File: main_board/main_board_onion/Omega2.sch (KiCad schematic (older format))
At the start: 25 parts, among them J16 RJ45, J17 USB_B_Micro_Omega, U4 H1102, U5 CP2102N-A01-GQFN24

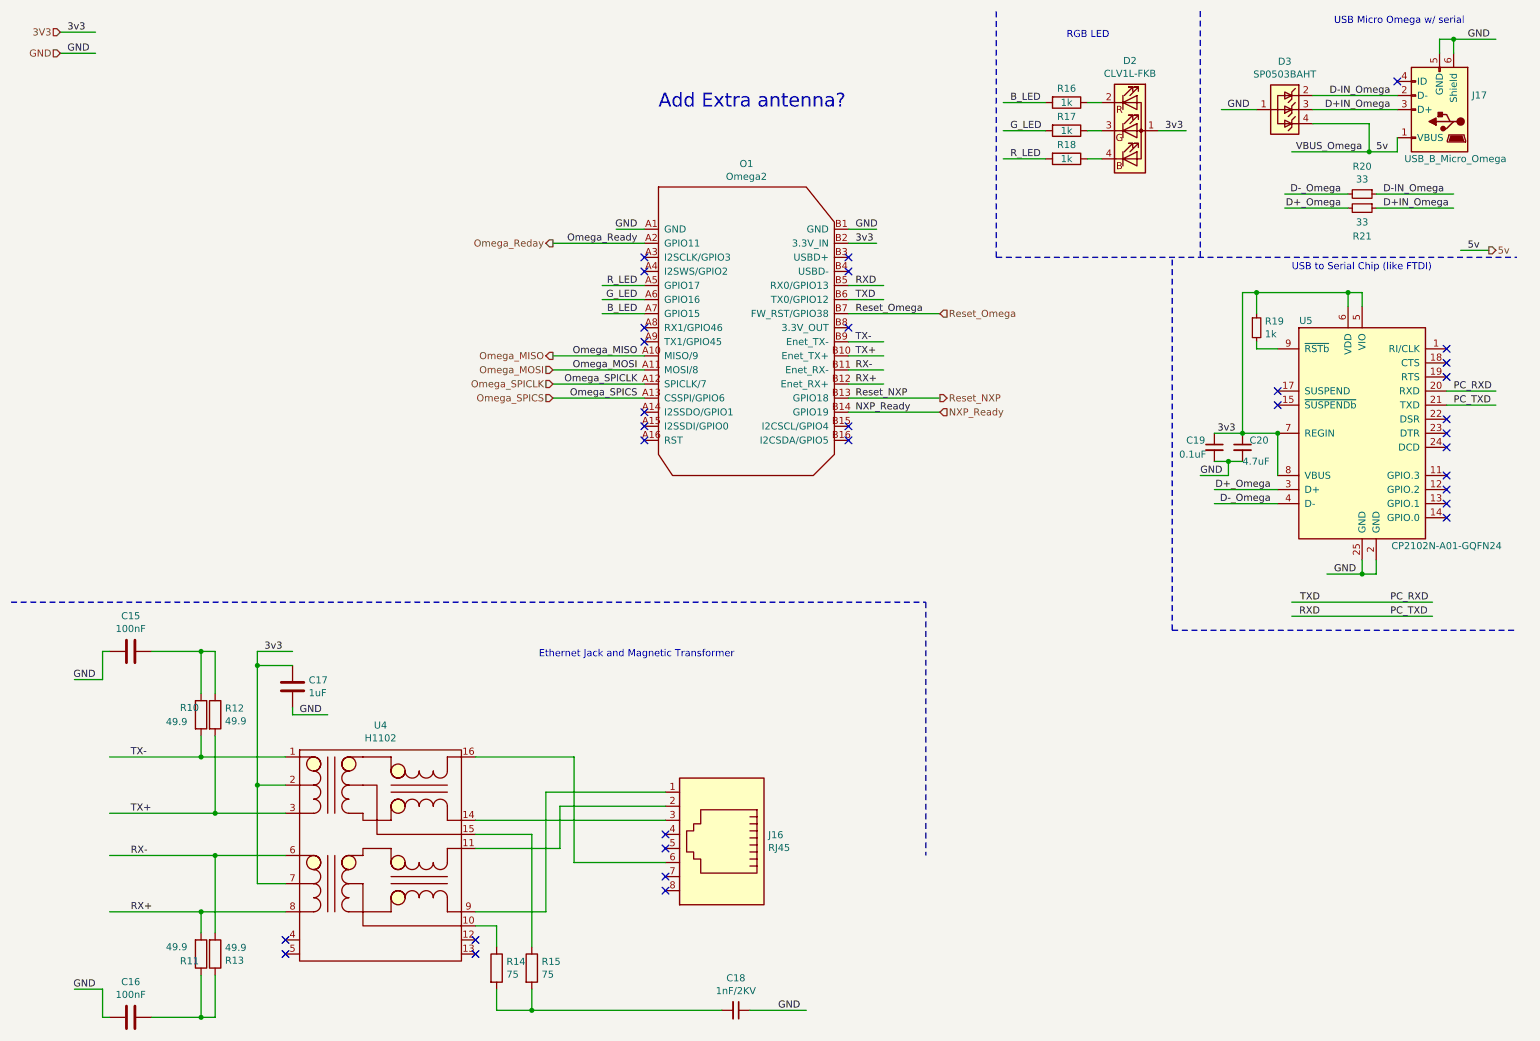
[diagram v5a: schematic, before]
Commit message: Init. from Onion_MacroFab_v2 branch and added Battery Monitor Testing files
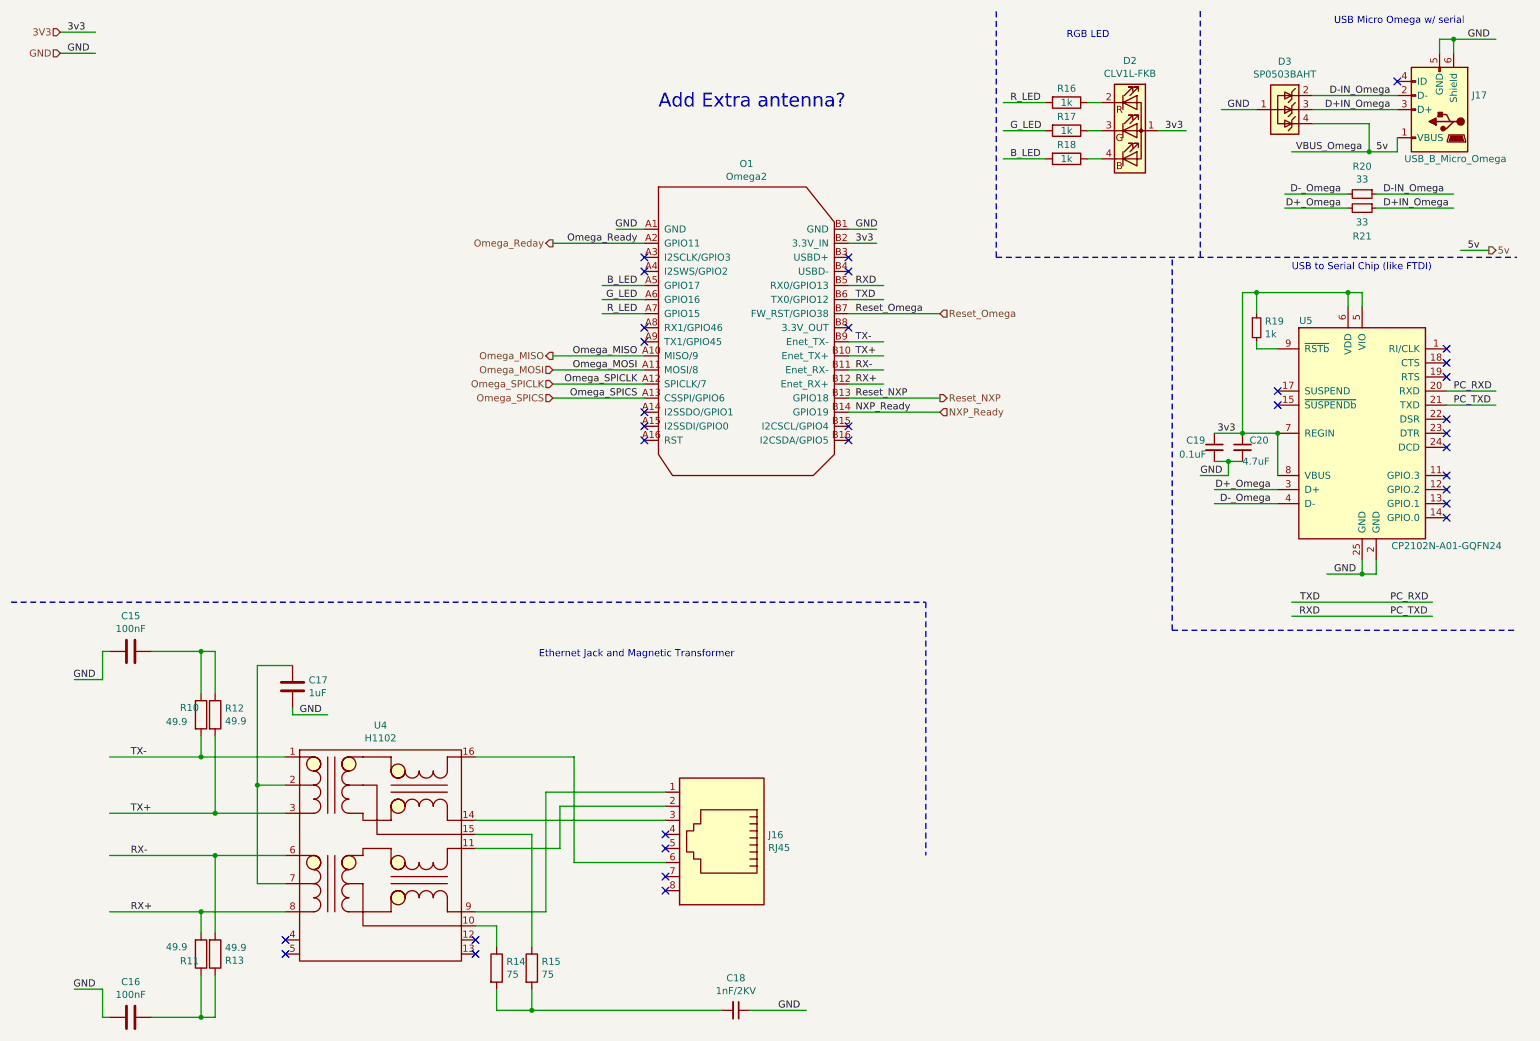
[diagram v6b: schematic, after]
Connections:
- wire segments 126 -> 124
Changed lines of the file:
@@
-EESchema Schematic File Version 4
+EESchema Schematic File Version 5
 LIBS:main_board_onion-cache
-EELAYER 26 0
+EELAYER 29 0
 EELAYER END
 $Descr A4 11693 8268
@@
 	8150 1150 8250 1150
 Text Label 4950 2650 2    50   ~ 0
-B_LED
+R_LED
 Text Label 4950 2550 2    50   ~ 0
 G_LED
 Text Label 4950 2450 2    50   ~ 0
-R_LED
+B_LED
 Wire Wire Line
 	5000 2450 4700 2450
@@
 	5000 2650 4700 2650
 Text Label 7600 1150 0    50   ~ 0
-B_LED
+R_LED
 Text Label 7600 1350 0    50   ~ 0
 G_LED
 Text Label 7600 1550 0    50   ~ 0
-R_LED
+B_LED
 Wire Wire Line
 	7550 1550 7850 1550
@@
 Wire Wire Line
 	2250 6000 2250 5150
-Wire Wire Line
-	2250 5050 2500 5050
 $Comp
 L Device:C C17
@@
 Wire Wire Line
 	2500 5150 2250 5150
-Connection ~ 2250 5150
-Wire Wire Line
-	2250 5150 2250 5050
 Wire Wire Line
 	2500 5450 2500 5500
@@
 Wire Wire Line
 	1850 6900 1200 6900
-Text Label 2300 5050 0    50   ~ 0
-3v3
 Text Label 6500 2850 0    50   ~ 0
 TX-

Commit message: Added Teensy and Battery monitoring designs to schematic
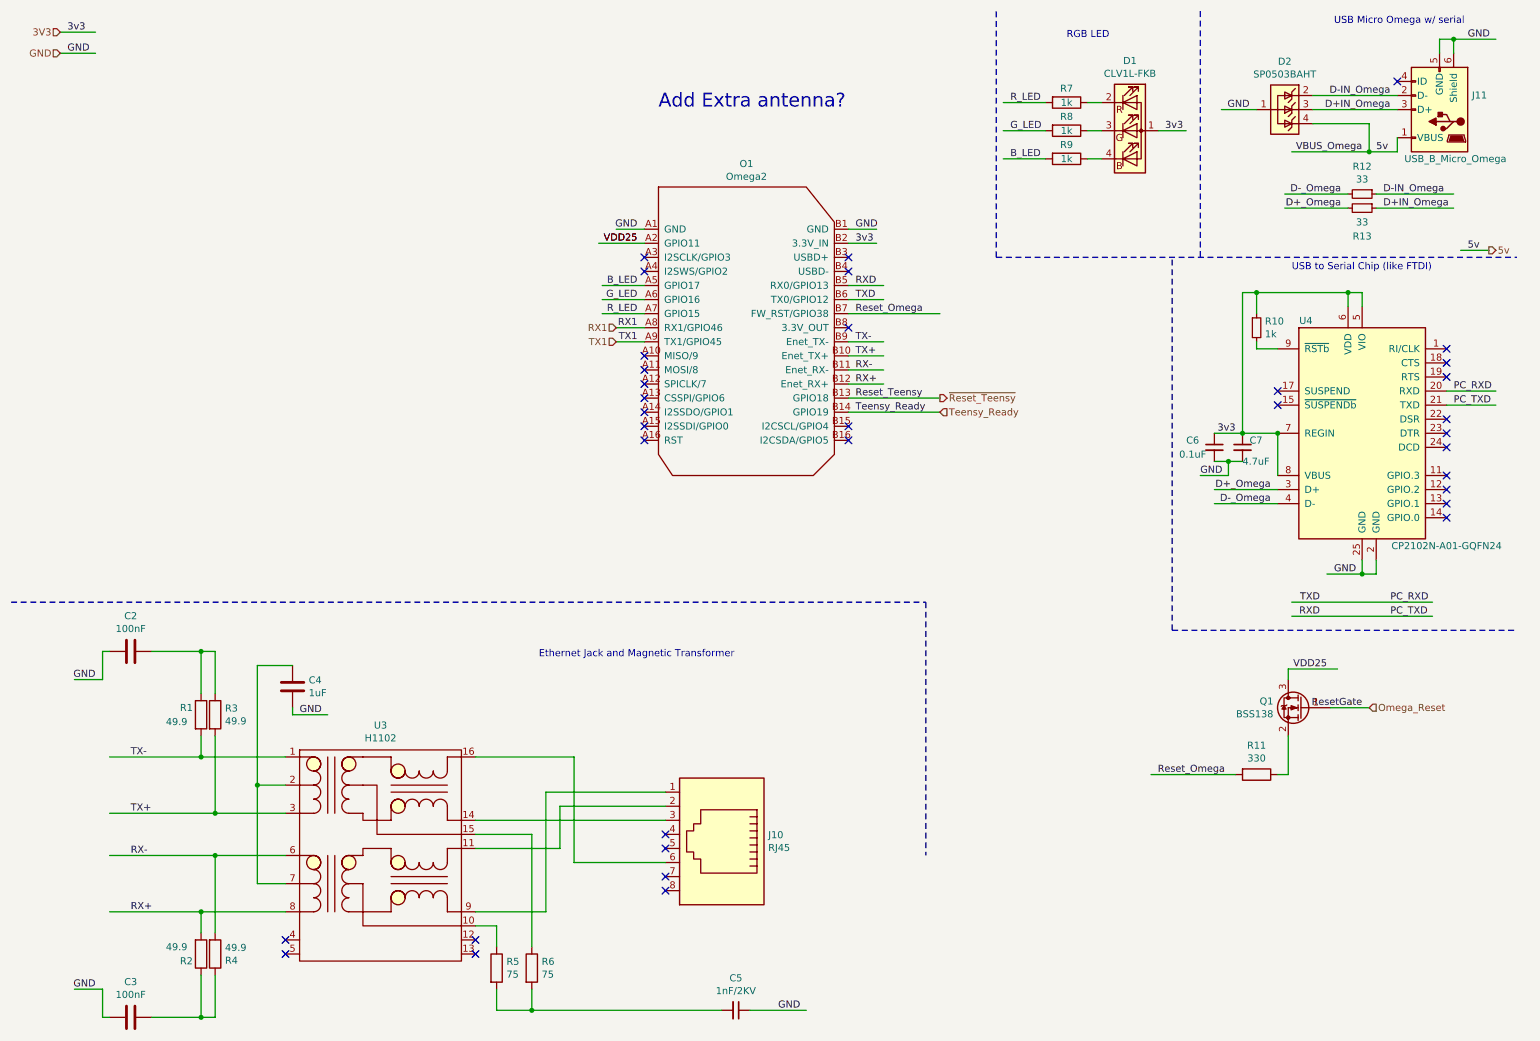
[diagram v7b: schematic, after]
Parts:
- added Q1: BSS138, Package_TO_SOT_SMD:SOT-23, symbol Transistor_FET:BSS138
- added R11: 330, Resistor_SMD:R_0603_1608Metric, symbol Device:R
- renumbered C15 to C2, C16 to C3, C17 to C4, C18 to C5, C19 to C6, C20 to C7, D2 to D1, D3 to D2, J16 to J10, J17 to J11, R10 to R1, R19 to R10, R20 to R12, R21 to R13, R11 to R2, R12 to R3, R13 to R4, R14 to R5, R15 to R6, R16 to R7, R17 to R8, R18 to R9, U4 to U3, U5 to U4
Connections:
- net labels added: Omega_Reset, RX1, ResetGate, Reset_Teensy, TX1, Teensy_Ready, VDD25, ~Reset_Teensy
- net labels removed: NXP_Ready, Omega_MISO, Omega_MOSI, Omega_Ready, Omega_Reday, Omega_SPICLK, Omega_SPICS, Reset_NXP
- wire segments 124 -> 128
- no-connect marks 33 -> 35
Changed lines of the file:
@@
 $Descr A4 11693 8268
 encoding utf-8
-Sheet 3 3
+Sheet 2 5
 Title ""
 Date ""
@@
 5v
 $Comp
-L Connector:USB_B_Micro J17
+L Connector:USB_B_Micro J11
 U 1 1 5B651845
 P 10650 1200
-F 0 "J17" H 10420 1098 50  0000 R CNN
+F 0 "J11" H 10420 1098 50  0000 R CNN
 F 1 "USB_B_Micro_Omega" H 10900 1550 50  0000 R CNN
 F 2 "Connector_USB:USB_Micro-B_Molex-105017-0001" H 10800 1150 50  0001 C CNN
@@
 USB Micro Omega w/ serial
 $Comp
-L Interface_USB:CP2102N-A01-GQFN24 U5
+L Interface_USB:CP2102N-A01-GQFN24 U4
 U 1 1 5B651CFD
 P 10100 3500
-F 0 "U5" H 9700 4300 50  0000 C CNN
+F 0 "U4" H 9700 4300 50  0000 C CNN
 F 1 "CP2102N-A01-GQFN24" H 10700 2700 50  0000 C CNN
 F 2 "Package_DFN_QFN:QFN-24-1EP_4x4mm_P0.5mm_EP2.6x2.6mm" H 10550 2700 50  0001 L CNN
@@
 	9050 3900 9500 3900
 $Comp
-L Device:C_Small C20
+L Device:C_Small C7
 U 1 1 5B652416
 P 9250 3600
-F 0 "C20" H 9300 3650 50  0000 L CNN
+F 0 "C7" H 9300 3650 50  0000 L CNN
 F 1 "4.7uF" H 9250 3500 50  0000 L CNN
 F 2 "Capacitor_SMD:C_0603_1608Metric" H 9250 3600 50  0001 C CNN
@@
 $EndComp
 $Comp
-L Device:C_Small C19
+L Device:C_Small C6
 U 1 1 5B652450
 P 9050 3600
-F 0 "C19" H 8850 3650 50  0000 L CNN
+F 0 "C6" H 8850 3650 50  0000 L CNN
 F 1 "0.1uF" H 8800 3550 50  0000 L CNN
 F 2 "Capacitor_SMD:C_0603_1608Metric" H 9050 3600 50  0001 C CNN
@@
 	10000 2500 10000 2600
 $Comp
-L Device:R_Small R19
+L Device:R_Small R10
 U 1 1 5B65310D
 P 9350 2750
-F 0 "R19" H 9409 2796 50  0000 L CNN
+F 0 "R10" H 9409 2796 50  0000 L CNN
 F 1 "1k" H 9409 2705 50  0000 L CNN
 F 2 "Resistor_SMD:R_0603_1608Metric" H 9350 2750 50  0001 C CNN
@@
 	9600 1500 10150 1500
 $Comp
-L main_board_onion-rescue:SP0503BAHT-Power_Protection D3
+L main_board_onion-rescue:SP0503BAHT-Power_Protection D2
 U 1 1 5B66BC75
 P 9550 1200
-F 0 "D3" V 9208 1200 50  0000 C CNN
+F 0 "D2" V 9208 1200 50  0000 C CNN
 F 1 "SP0503BAHT" V 9299 1200 50  0000 C CNN
 F 2 "Package_TO_SOT_SMD:SOT-143" H 9775 1150 50  0001 L CNN
@@
 D+IN_Omega
 $Comp
-L Device:R_Small R20
+L Device:R_Small R12
 U 1 1 5B69A77B
 P 10100 1800
-F 0 "R20" V 9904 1800 50  0000 C CNN
+F 0 "R12" V 9904 1800 50  0000 C CNN
 F 1 "33" V 9995 1800 50  0000 C CNN
 F 2 "Resistor_SMD:R_0603_1608Metric" H 10100 1800 50  0001 C CNN
@@
 $EndComp
 $Comp
-L Device:R_Small R21
+L Device:R_Small R13
 U 1 1 5B69A7E8
 P 10100 1900
-F 0 "R21" V 10300 1900 50  0000 C CNN
+F 0 "R13" V 10300 1900 50  0000 C CNN
 F 1 "33" V 10200 1900 50  0000 C CNN
 F 2 "Resistor_SMD:R_0603_1608Metric" H 10100 1900 50  0001 C CNN
@@
 Text Label 9450 3900 2    50   ~ 0
 D+_Omega
-Text Label 6500 2550 0    50   ~ 0
-TXD
 Text Label 6500 2450 0    50   ~ 0
 RXD
@@
 	6450 2550 6700 2550
 $Comp
-L LED:CLV1L-FKB D2
+L LED:CLV1L-FKB D1
 U 1 1 5B6A8E1C
 P 8450 1350
-F 0 "D2" H 8450 1847 50  0000 C CNN
+F 0 "D1" H 8450 1847 50  0000 C CNN
 F 1 "CLV1L-FKB" H 8450 1756 50  0000 C CNN
 F 2 "LED_SMD:LED_Cree-PLCC4_3.2x2.8mm_CCW" H 8450 1300 50  0001 C CNN
@@
 3v3
 $Comp
-L Device:R R16
+L Device:R R7
 U 1 1 5B6AA8B8
 P 8000 1150
-F 0 "R16" V 7900 1150 50  0000 C CNN
+F 0 "R7" V 7900 1150 50  0000 C CNN
 F 1 "1k" V 8000 1150 50  0000 C CNN
 F 2 "Resistor_SMD:R_0603_1608Metric" V 7930 1150 50  0001 C CNN
@@
 $EndComp
 $Comp
-L Device:R R17
+L Device:R R8
 U 1 1 5B6AA9DD
 P 8000 1350
-F 0 "R17" V 7900 1350 50  0000 C CNN
+F 0 "R8" V 7900 1350 50  0000 C CNN
 F 1 "1k" V 8000 1350 50  0000 C CNN
 F 2 "Resistor_SMD:R_0603_1608Metric" V 7930 1350 50  0001 C CNN
@@
 $EndComp
 $Comp
-L Device:R R18
+L Device:R R9
 U 1 1 5B6AAA0D
 P 8000 1550
-F 0 "R18" V 7900 1550 50  0000 C CNN
+F 0 "R9" V 7900 1550 50  0000 C CNN
 F 1 "1k" V 8000 1550 50  0000 C CNN
 F 2 "Resistor_SMD:R_0603_1608Metric" V 7930 1550 50  0001 C CNN
@@
 	7500 2250 11200 2250
 $Comp
-L Pulse:H1102 U4
+L Pulse:H1102 U3
 U 1 1 5B6C2CE9
 P 3100 6450
-F 0 "U4" H 3125 7325 50  0000 C CNN
+F 0 "U3" H 3125 7325 50  0000 C CNN
 F 1 "H1102" H 3125 7234 50  0000 C CNN
 F 2 "Package_SO:SOIC-16W_7.5x12.8mm_P1.27mm" H 2800 6750 50  0001 C CNN
@@
 	4300 6900 3800 6900
 $Comp
-L Device:R R14
+L Device:R R5
 U 1 1 5B6CE392
 P 3950 7300
-F 0 "R14" H 4020 7346 50  0000 L CNN
+F 0 "R5" H 4020 7346 50  0000 L CNN
 F 1 "75" H 4020 7255 50  0000 L CNN
 F 2 "Resistor_SMD:R_0603_1608Metric" V 3880 7300 50  0001 C CNN
@@
 $EndComp
 $Comp
-L Device:R R15
+L Device:R R6
 U 1 1 5B6CE45E
 P 4200 7300
-F 0 "R15" H 4270 7346 50  0000 L CNN
+F 0 "R6" H 4270 7346 50  0000 L CNN
 F 1 "75" H 4270 7255 50  0000 L CNN
 F 2 "Resistor_SMD:R_0603_1608Metric" V 4130 7300 50  0001 C CNN
@@
 Connection ~ 4200 7600
 $Comp
-L Device:C_Small C18
+L Device:C_Small C5
 U 1 1 5B6D6417
 P 5650 7600
-F 0 "C18" V 5421 7600 50  0000 C CNN
+F 0 "C5" V 5421 7600 50  0000 C CNN
 F 1 "1nF/2KV" V 5512 7600 50  0000 C CNN
 F 2 "Capacitor_SMD:C_0603_1608Metric" H 5650 7600 50  0001 C CNN
@@
 NoConn ~ 5150 6750
 $Comp
-L Device:R R10
+L Device:R R1
 U 1 1 5B6EE2BA
 P 1850 5500
-F 0 "R10" H 1700 5550 50  0000 L CNN
+F 0 "R1" H 1700 5550 50  0000 L CNN
 F 1 "49.9" H 1600 5450 50  0000 L CNN
 F 2 "Resistor_SMD:R_0603_1608Metric" V 1780 5500 50  0001 C CNN
@@
 $EndComp
 $Comp
-L Device:R R12
+L Device:R R3
 U 1 1 5B6EE3D5
 P 1950 5500
-F 0 "R12" H 2020 5546 50  0000 L CNN
+F 0 "R3" H 2020 5546 50  0000 L CNN
 F 1 "49.9" H 2020 5455 50  0000 L CNN
 F 2 "Resistor_SMD:R_0603_1608Metric" V 1880 5500 50  0001 C CNN
@@
 $EndComp
 $Comp
-L Device:C C15
+L Device:C C2
 U 1 1 5B6EE44E
 P 1350 5050
-F 0 "C15" V 1098 5050 50  0000 C CNN
+F 0 "C2" V 1098 5050 50  0000 C CNN
 F 1 "100nF" V 1189 5050 50  0000 C CNN
 F 2 "Capacitor_SMD:C_0603_1608Metric" H 1388 4900 50  0001 C CNN
@@
 	2250 6000 2250 5150
 $Comp
-L Device:C C17
+L Device:C C4
 U 1 1 5B716833
 P 2500 5300
-F 0 "C17" H 2385 5254 50  0000 R CNN
+F 0 "C4" H 2385 5254 50  0000 R CNN
 F 1 "1uF" H 2385 5345 50  0000 R CNN
 F 2 "Capacitor_SMD:C_0603_1608Metric" H 2538 5150 50  0001 C CNN
@@
 RX+
 $Comp
-L Device:R R11
+L Device:R R2
 U 1 1 5B7228FD
 P 1850 7200
-F 0 "R11" H 1700 7250 50  0000 L CNN
+F 0 "R2" H 1700 7250 50  0000 L CNN
 F 1 "49.9" H 1600 7150 50  0000 L CNN
 F 2 "Resistor_SMD:R_0603_1608Metric" V 1780 7200 50  0001 C CNN
@@
 $EndComp
 $Comp
-L Device:R R13
+L Device:R R4
 U 1 1 5B722904
 P 1950 7200
-F 0 "R13" H 2020 7246 50  0000 L CNN
+F 0 "R4" H 2020 7246 50  0000 L CNN
 F 1 "49.9" H 2020 7155 50  0000 L CNN
 F 2 "Resistor_SMD:R_0603_1608Metric" V 1880 7200 50  0001 C CNN
@@
 $EndComp
 $Comp
-L Device:C C16
+L Device:C C3
 U 1 1 5B72290B
 P 1350 7650
-F 0 "C16" V 1602 7650 50  0000 C CNN
+F 0 "C3" V 1602 7650 50  0000 C CNN
 F 1 "100nF" V 1511 7650 50  0000 C CNN
 F 2 "Capacitor_SMD:C_0603_1608Metric" H 1388 7500 50  0001 C CNN
@@
 Text Label 6500 2650 0    50   ~ 0
 Reset_Omega
-Text Label 4950 2950 2    50   ~ 0
-Omega_MISO
-Text Label 4950 3050 2    50   ~ 0
-Omega_MOSI
-Text Label 4950 3150 2    50   ~ 0
-Omega_SPICLK
-Wire Wire Line
-	5000 3150 4350 3150
-Wire Wire Line
-	5000 3050 4350 3050
-Wire Wire Line
-	5000 2950 4350 2950
-Text Label 4950 3250 2    50   ~ 0
-Omega_SPICS
-Wire Wire Line
-	5000 3250 4350 3250
 NoConn ~ 6450 2250
 NoConn ~ 6450 2350
@@
 NoConn ~ 5000 3550
 Text Label 6500 3250 0    50   ~ 0
-Reset_NXP
+Reset_Teensy
 Text Label 6500 3350 0    50   ~ 0
-NXP_Ready
+Teensy_Ready
 Wire Wire Line
 	6450 3250 7100 3250
 Wire Wire Line
 	6450 3350 7100 3350
-Text Label 4950 2150 2    50   ~ 0
-Omega_Ready
 NoConn ~ 5000 2250
 NoConn ~ 5000 2350
-NoConn ~ 5000 2750
-NoConn ~ 5000 2850
+NoConn ~ 5000 3050
+NoConn ~ 5000 2950
 NoConn ~ 5000 3350
 NoConn ~ 5000 3450
 NoConn ~ 6450 3450
 NoConn ~ 6450 3550
-Text HLabel 4350 2950 0    50   Output ~ 0
-Omega_MISO
-Text HLabel 4350 3050 0    50   Input ~ 0
-Omega_MOSI
-Text HLabel 4350 3150 0    50   Input ~ 0
-Omega_SPICLK
-Text HLabel 4350 3250 0    50   Input ~ 0
-Omega_SPICS
-Text HLabel 4350 2150 0    50   Output ~ 0
-Omega_Reday
-Wire Wire Line
-	4350 2150 5000 2150
-Text HLabel 7100 2650 2    50   Input ~ 0
-Reset_Omega
 Wire Wire Line
 	6450 2650 7100 2650
 Text HLabel 7100 3350 2    50   Input ~ 0
-NXP_Ready
+Teensy_Ready
 Text HLabel 7100 3250 2    50   Output ~ 0
-Reset_NXP
+~Reset_Teensy
 Text Notes 5100 1200 0    98   ~ 0
 Add Extra antenna?
 $Comp
-L Connector:RJ45 J16
+L Connector:RJ45 J10
 U 1 1 5B6A0DFB
 P 5550 6350
-F 0 "J16" H 5220 6354 50  0000 R CNN
+F 0 "J10" H 5220 6354 50  0000 R CNN
 F 1 "RJ45" H 5220 6445 50  0000 R CNN
 F 2 "TE:1-338088-3" V 5550 6375 50  0001 C CNN
@@
 	4200 7600 5550 7600
 Connection ~ 9500 3500
+Text Label 6500 2550 0    50   ~ 0
+TXD
+Text Label 4950 2750 2    50   ~ 0
+RX1
+Text Label 4950 2850 2    50   ~ 0
+TX1
+Wire Wire Line
+	5000 2850 4800 2850
+Wire Wire Line
+	5000 2750 4800 2750
+NoConn ~ 5000 3150
+NoConn ~ 5000 3250
+Text HLabel 4800 2750 0    50   Input ~ 0
+RX1
+Text HLabel 4800 2850 0    50   Input ~ 0
+TX1
+Text Label 4950 2150 2    50   ~ 0
+VDD25
+Wire Wire Line
+	5000 2150 4675 2150
+Text Label 4950 2150 2    50   ~ 0
+VDD25
+Wire Wire Line
+	9200 5925 8600 5925
+Wire Wire Line
+	9575 5250 9575 5175
+Wire Wire Line
+	9575 5175 9925 5175
+Wire Wire Line
+	9500 5925 9575 5925
+Wire Wire Line
+	9575 5925 9575 5650
+$Comp
+L Device:R R11
+U 1 1 5D0274A7
+P 9350 5925
+F 0 "R11" V 9143 5925 50  0000 C CNN
+F 1 "330" V 9234 5925 50  0000 C CNN
+F 2 "Resistor_SMD:R_0603_1608Metric" V 9280 5925 50  0001 C CNN
+F 3 "~" H 9350 5925 50  0001 C CNN
+	1    9350 5925
+	0    1    1    0
+$EndComp
+$Comp
+L Transistor_FET:BSS138 Q1
+U 1 1 5D02392E
+P 9675 5450
+F 0 "Q1" H 9881 5496 50  0000 L CNN
+F 1 "BSS138" H 9881 5405 50  0000 L CNN
+F 2 "Package_TO_SOT_SMD:SOT-23" H 9875 5375 50  0001 L CIN
+F 3 "https://www.fairchildsemi.com/datasheets/BS/BSS138.pdf" H 9675 5450 50  0001 L CNN
+	1    9675 5450
+	-1   0    0    -1
+$EndComp
+Text Label 9125 5925 2    50   ~ 0
+Reset_Omega
+Wire Wire Line
+	9875 5450 10150 5450
+Text Label 9850 5175 2    50   ~ 0
+VDD25
+Text HLabel 10150 5450 2    50   Input ~ 0
+Omega_Reset
+Text Label 10100 5450 2    50   ~ 0
+ResetGate
 $EndSCHEMATC
